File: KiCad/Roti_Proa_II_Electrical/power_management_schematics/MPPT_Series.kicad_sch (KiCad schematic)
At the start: 19 parts, among them SW1 SW_DIP_x02, SW2 SW_DIP_x02

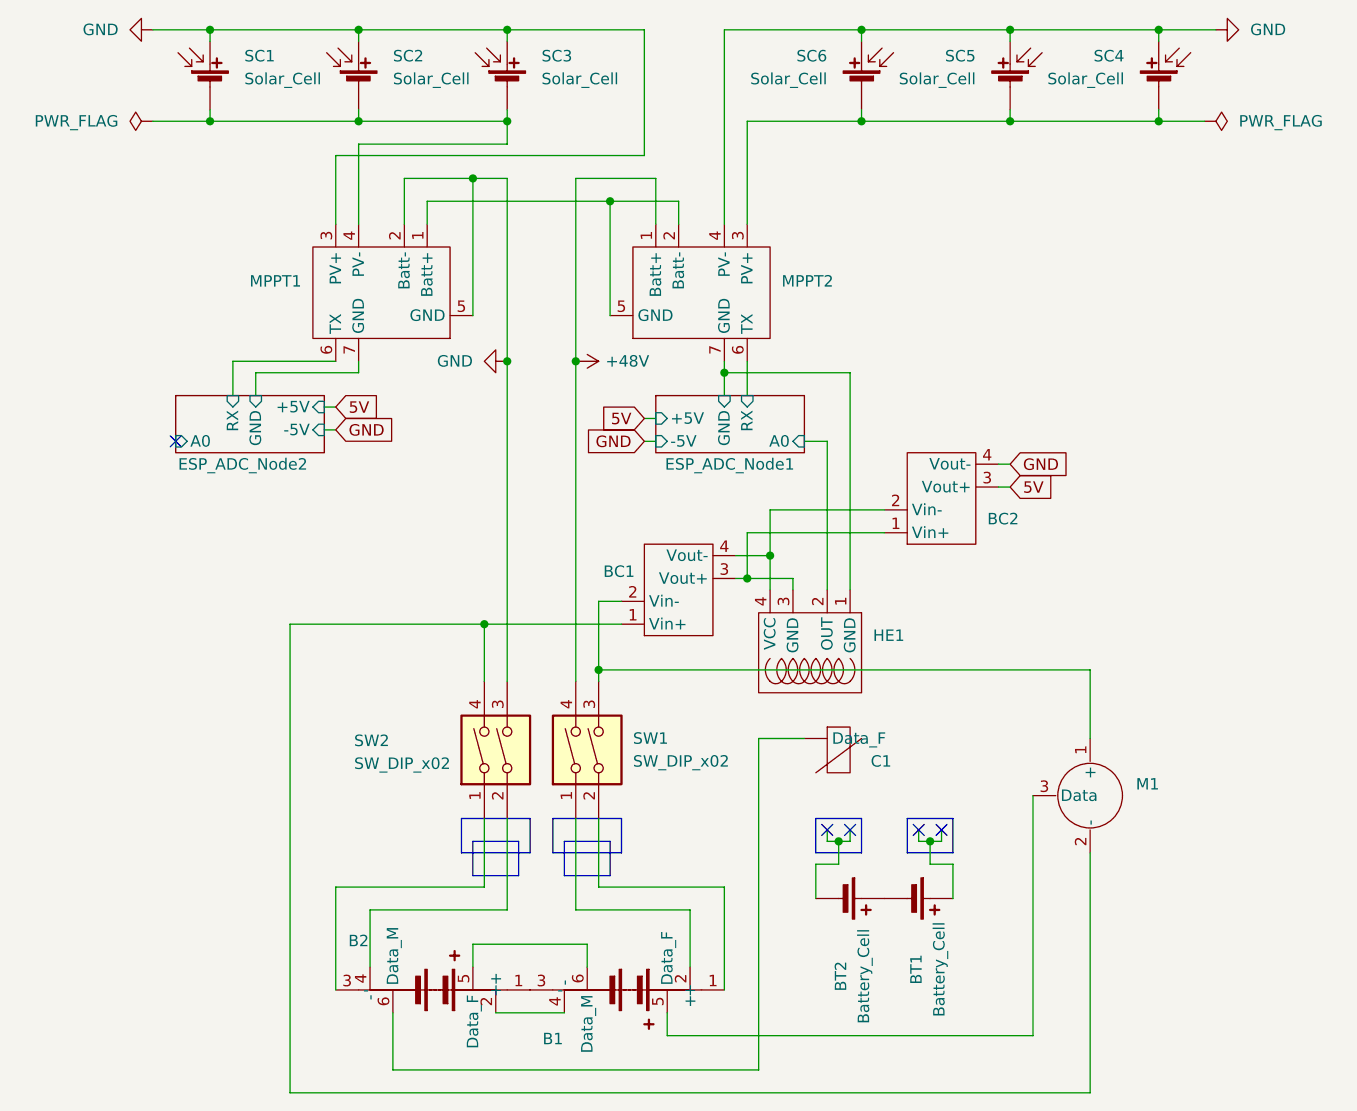
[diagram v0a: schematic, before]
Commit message: Complete MPPT+HE reading
Reading works for arduino and esp8266
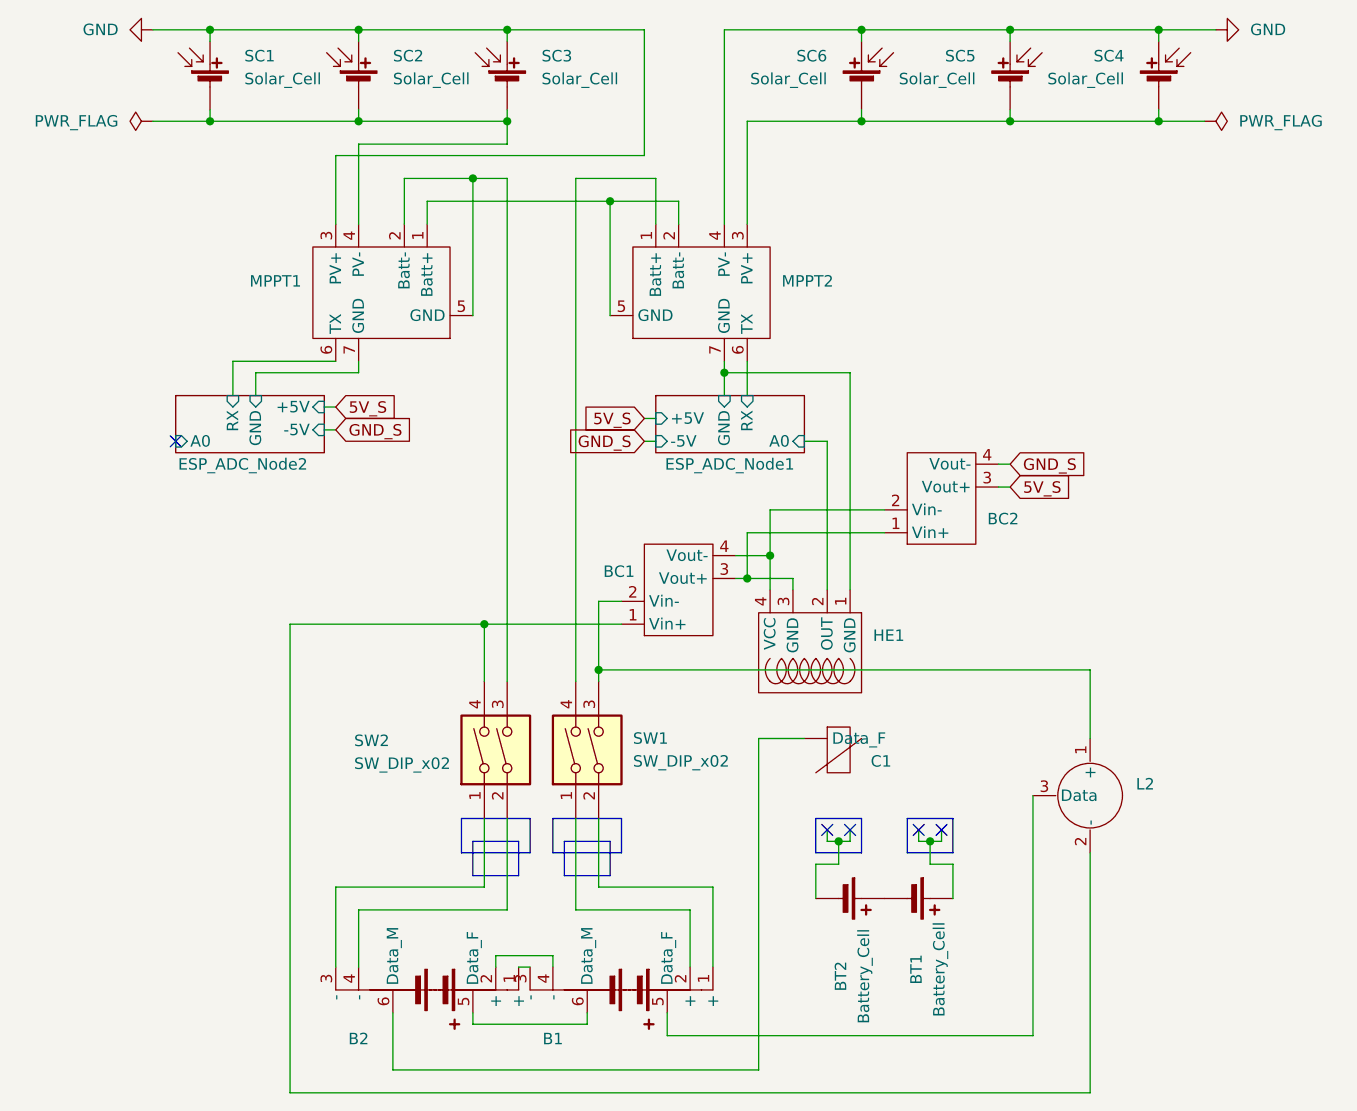
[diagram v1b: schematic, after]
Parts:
- removed M1: ~, symbol Proa2_v2:Motor
- added L2: ~, symbol Proa2_v2:Motor
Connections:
- net GND: no longer BC2.4 (Vout-), MPPT1.2 (Batt-), MPPT1.5 (GND), SW2.3
- net at BC1.2 (Vin-), SW1.3: now also L2.1 (+)
- net at BC1.1 (Vin+), SW2.4: now also L2.2 (-)
- net at B1.5 (Data_F): now also L2.3 (Data)
- net +48V: no longer names the net of MPPT2.1 (Batt+), SW1.4
- net 5V renamed 5V_S
- new net: MPPT1.2 (Batt-), MPPT1.5 (GND), SW2.3
- new net GND_S: BC2.4 (Vout-)
